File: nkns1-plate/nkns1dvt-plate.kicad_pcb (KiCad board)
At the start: 2 copper layers, 170.7 x 126.8 mm, 2 parts

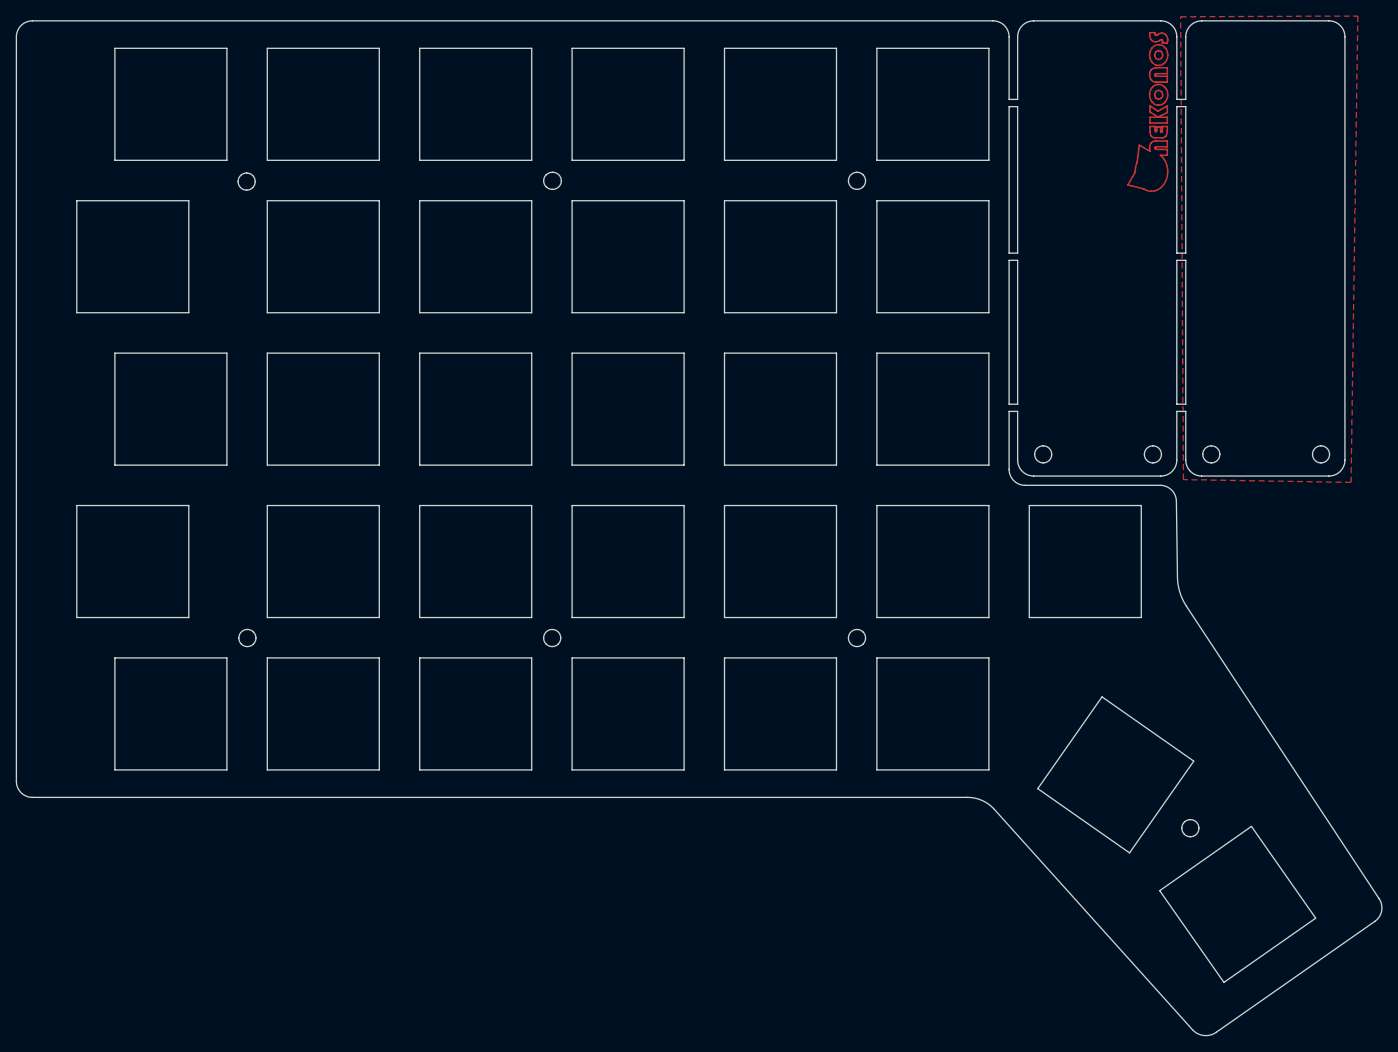
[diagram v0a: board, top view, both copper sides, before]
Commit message: Modify to plated key holes (nkns1-plate)
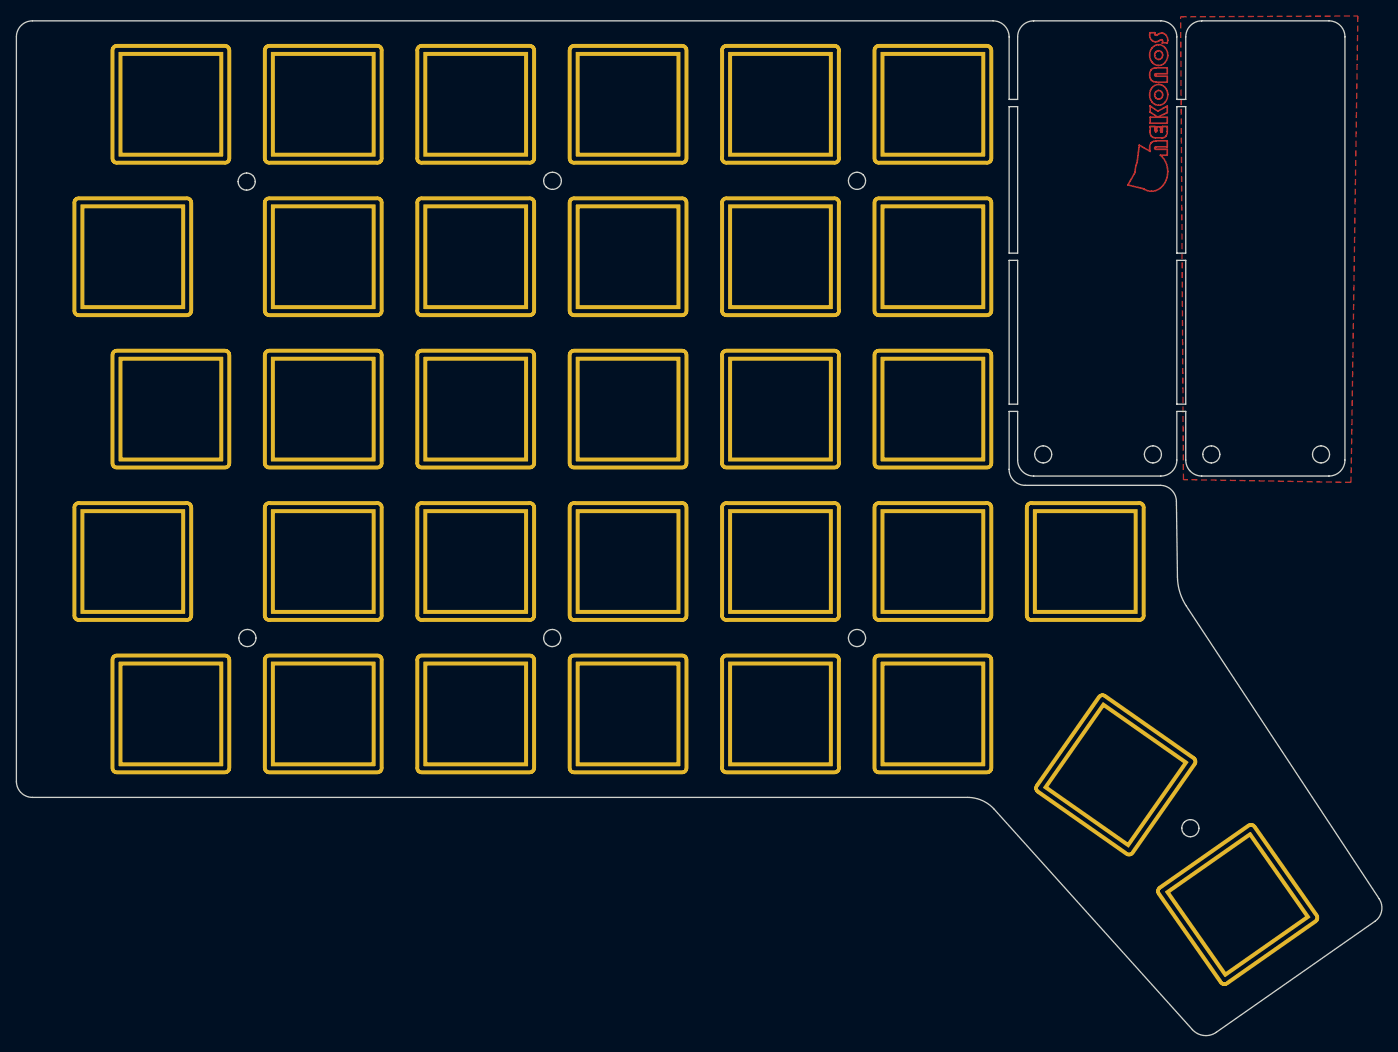
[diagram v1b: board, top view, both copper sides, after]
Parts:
- added SW2: KEY_SWITCH, kbd:SW_Hole_TH, F.Cu at (177.2, 136.7)
- added SW2: KEY_SWITCH, kbd:SW_Hole_TH, F.Cu at (139.1, 93.9)
- added SW2: KEY_SWITCH, kbd:SW_Hole_TH, F.Cu at (120.0, 93.9)
- added SW2: KEY_SWITCH, kbd:SW_Hole_TH, F.Cu at (101.0, 93.9)
- added SW2: KEY_SWITCH, kbd:SW_Hole_TH, F.Cu at (81.9, 93.9)
- added SW2: KEY_SWITCH, kbd:SW_Hole_TH, F.Cu at (62.9, 93.9)
- added SW2: KEY_SWITCH, kbd:SW_Hole_TH, F.Cu at (39.0, 93.9)
- added SW2: KEY_SWITCH, kbd:SW_Hole_TH, F.Cu at (139.1, 74.8)
- added SW2: KEY_SWITCH, kbd:SW_Hole_TH, F.Cu at (120.0, 74.8)
- added SW2: KEY_SWITCH, kbd:SW_Hole_TH, F.Cu at (101.0, 74.8)
- added SW2: KEY_SWITCH, kbd:SW_Hole_TH, F.Cu at (81.9, 74.8)
- added SW2: KEY_SWITCH, kbd:SW_Hole_TH, F.Cu at (161.9, 120.5)
- added SW2: KEY_SWITCH, kbd:SW_Hole_TH, F.Cu at (62.9, 74.8)
- added SW2: KEY_SWITCH, kbd:SW_Hole_TH, F.Cu at (43.8, 74.8)
- added SW2: KEY_SWITCH, kbd:SW_Hole_TH, F.Cu at (139.1, 55.8)
- added SW2: KEY_SWITCH, kbd:SW_Hole_TH, F.Cu at (120.0, 55.8)
- added SW2: KEY_SWITCH, kbd:SW_Hole_TH, F.Cu at (101.0, 55.8)
- added SW2: KEY_SWITCH, kbd:SW_Hole_TH, F.Cu at (81.9, 55.8)
- added SW2: KEY_SWITCH, kbd:SW_Hole_TH, F.Cu at (62.9, 55.8)
- added SW2: KEY_SWITCH, kbd:SW_Hole_TH, F.Cu at (39.0, 55.8)
- added SW2: KEY_SWITCH, kbd:SW_Hole_TH, F.Cu at (139.1, 36.7)
- added SW2: KEY_SWITCH, kbd:SW_Hole_TH, F.Cu at (120.0, 36.7)
- added SW2: KEY_SWITCH, kbd:SW_Hole_TH, F.Cu at (43.8, 112.9)
- added SW2: KEY_SWITCH, kbd:SW_Hole_TH, F.Cu at (101.0, 36.7)
- added SW2: KEY_SWITCH, kbd:SW_Hole_TH, F.Cu at (81.9, 36.7)
- added SW2: KEY_SWITCH, kbd:SW_Hole_TH, F.Cu at (62.9, 36.7)
- added SW2: KEY_SWITCH, kbd:SW_Hole_TH, F.Cu at (43.8, 36.7)
- added SW2: KEY_SWITCH, kbd:SW_Hole_TH, F.Cu at (62.9, 112.9)
- added SW2: KEY_SWITCH, kbd:SW_Hole_TH, F.Cu at (81.9, 112.9)
- added SW2: KEY_SWITCH, kbd:SW_Hole_TH, F.Cu at (101.0, 112.9)
- added SW2: KEY_SWITCH, kbd:SW_Hole_TH, F.Cu at (120.0, 112.9)
- added SW2: KEY_SWITCH, kbd:SW_Hole_TH, F.Cu at (139.1, 112.9)
- added SW2: KEY_SWITCH, kbd:SW_Hole_TH, F.Cu at (158.1, 93.9)
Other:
- outline, holes or cut-outs redrawn
